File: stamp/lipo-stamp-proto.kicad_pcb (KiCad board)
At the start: 4 copper layers, 17.8 x 17.8 mm, 31 parts, among them IC1 TP4056, Q1 Q_PMOS_GSD, U1 AP2112K-3.3, U2 AP9101CK6, U3 FS8205

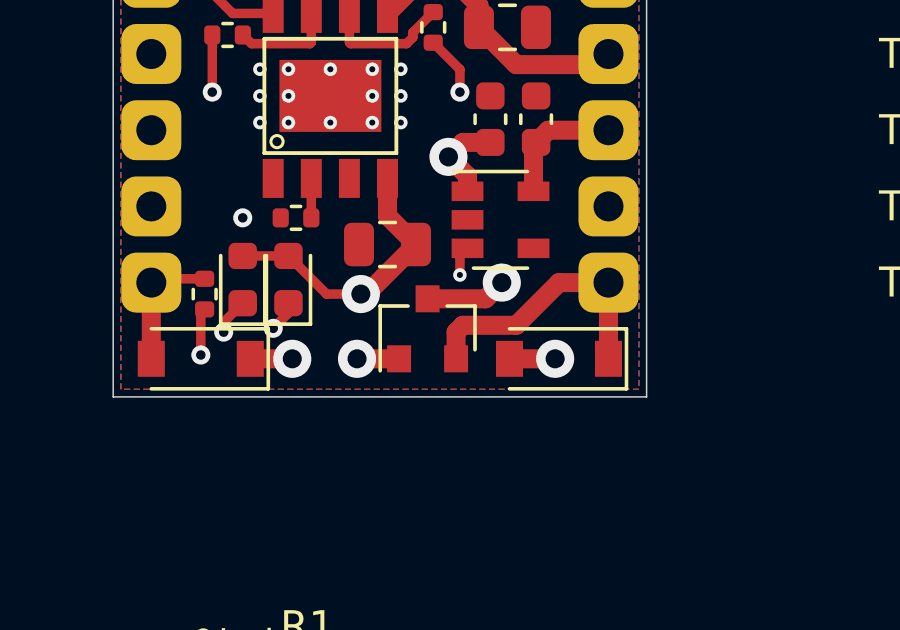
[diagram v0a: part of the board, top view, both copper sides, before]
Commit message: Add fabrication outputs, not jlc corrected yet
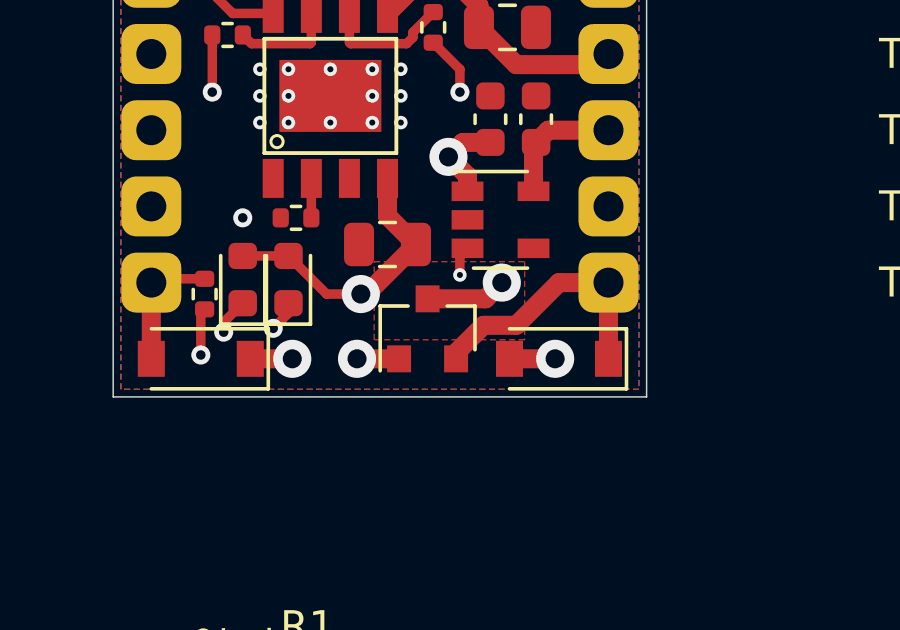
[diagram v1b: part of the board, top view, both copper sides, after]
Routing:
- added copper zone on F.Cu, net /+BATT
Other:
- board text added: "@bitshiftmask"
- board text added: "IN"
- board text added: "JLCJLCJLCJLC"
- board text added: "LiPo Stamp v0.3.0"
- board text added: "OUT"
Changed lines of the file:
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@@
   (general
     (thickness 1.6)
-    (drawings 16)
+    (drawings 31)
     (tracks 163)
     (zones 0)
@@
   )
   (setup
-    (last_trace_width 0.25)
+    (last_trace_width 0.635)
     (user_trace_width 0.2)
     (user_trace_width 0.3175)
@@
       (outputformat 1)
       (mirror false)
-      (drillshape 1)
+      (drillshape 0)
       (scaleselection 1)
-      (outputdirectory ""))
+      (outputdirectory "../fabrication/stamp/"))
   )
   (net 0 "")
@@
   (module Everything:SOP-8 (layer F.Cu)
     (at 115.189 58.547 90)
+    (attr smd)
     (fp_text reference IC1 (at 0.381 -23.241 90) (layer F.SilkS)
       (effects (font (size 1.000283 1.000283) (thickness 0.015)))
@@
     )
   )
+  (gr_text OUT (at 124.079 52.07) (layer B.SilkS)
+    (effects (font (size 1 1) (thickness 0.15)) (justify mirror))
+  )
+  (gr_text IN (at 109.22 52.07) (layer B.SilkS)
+    (effects (font (size 1 1) (thickness 0.15)) (justify mirror))
+  )
+  (gr_line (start 111.506 65.786) (end 122.428 65.786) (layer B.SilkS) (width 0.12))
+  (gr_line (start 111.506 67.564) (end 111.506 65.786) (layer B.SilkS) (width 0.12))
+  (gr_line (start 122.428 67.564) (end 111.506 67.564) (layer B.SilkS) (width 0.12))
+  (gr_line (start 122.428 65.786) (end 122.428 67.564) (layer B.SilkS) (width 0.12))
+  (gr_line (start 114.3 58.42) (end 114.3 53.34) (layer B.SilkS) (width 0.12))
+  (gr_line (start 119.38 58.42) (end 114.3 58.42) (layer B.SilkS) (width 0.12))
+  (gr_line (start 119.38 53.34) (end 119.38 58.42) (layer B.SilkS) (width 0.12))
+  (gr_line (start 111.379 53.34) (end 111.379 51.054) (layer B.SilkS) (width 0.12))
+  (gr_line (start 122.301 53.34) (end 111.379 53.34) (layer B.SilkS) (width 0.12))
+  (gr_line (start 122.301 51.054) (end 122.301 53.34) (layer B.SilkS) (width 0.12))
+  (gr_text @bitshiftmask (at 116.84 66.675) (layer B.SilkS)
+    (effects (font (size 1 1) (thickness 0.15)) (justify mirror))
+  )
+  (gr_text "LiPo\nStamp\nv0.3.0" (at 116.84 55.88) (layer B.SilkS)
+    (effects (font (size 1 1) (thickness 0.15)) (justify mirror))
+  )
+  (gr_text JLCJLCJLCJLC (at 116.84 52.07) (layer B.SilkS)
+    (effects (font (size 1 1) (thickness 0.15)) (justify mirror))
+  )
   (gr_text VMAX (at 123.19 64.77) (layer B.SilkS)
     (effects (font (size 1 1) (thickness 0.15)) (justify left mirror))
@@
     (effects (font (size 1 1) (thickness 0.15)) (justify right mirror))
   )
-  (gr_text B+ (at 110.49 57.15) (layer B.SilkS)
-    (effects (font (size 1 1) (thickness 0.15)) (justify right mirror))
-  )
-  (gr_text B- (at 111.76 54.61) (layer B.SilkS)
-    (effects (font (size 1 1) (thickness 0.15)) (justify right mirror))
+  (gr_text B+ (at 113.665 57.15) (layer B.SilkS)
+    (effects (font (size 1 1) (thickness 0.15)) (justify left mirror))
+  )
+  (gr_text B- (at 113.665 54.61) (layer B.SilkS)
+    (effects (font (size 1 1) (thickness 0.15)) (justify left mirror))
   )
   (gr_line (start 125.73 50.8) (end 107.95 50.8) (layer Edge.Cuts) (width 0.05))
@@
   (segment (start 110.998 64.643) (end 109.347 64.643) (width 0.3175) (layer F.Cu) (net 8))
   (segment (start 124.46 67.31) (end 124.46 64.77) (width 0.635) (layer F.Cu) (net 9))
-  (segment (start 119.38 67.31) (end 119.38 66.421) (width 0.635) (layer F.Cu) (net 9))
-  (segment (start 119.608501 66.192499) (end 121.386501 66.192499) (width 0.635) (layer F.Cu) (net 9))
-  (segment (start 119.38 66.421) (end 119.608501 66.192499) (width 0.635) (layer F.Cu) (net 9))
   (segment (start 122.809 64.77) (end 124.46 64.77) (width 0.635) (layer F.Cu) (net 9))
   (segment (start 121.386501 66.192499) (end 122.809 64.77) (width 0.635) (layer F.Cu) (net 9))
@@
   (segment (start 124.46 64.77) (end 123.317 64.77) (width 1.27) (layer In1.Cu) (net 9))
   (segment (start 123.317 64.77) (end 119.126 60.579) (width 1.27) (layer In1.Cu) (net 9))
+  (segment (start 119.38 67.108498) (end 119.38 67.31) (width 0.635) (layer F.Cu) (net 9))
+  (segment (start 120.295999 66.192499) (end 119.38 67.108498) (width 0.635) (layer F.Cu) (net 9))
+  (segment (start 121.386501 66.192499) (end 120.295999 66.192499) (width 0.635) (layer F.Cu) (net 9))
   (segment (start 109.22 52.126) (end 109.164 52.07) (width 0.635) (layer F.Cu) (net 10))
   (segment (start 109.22 54.61) (end 109.22 52.126) (width 0.635) (layer F.Cu) (net 10))
@@
       )
     )
+  )
+  (zone (net 3) (net_name /+BATT) (layer F.Cu) (hatch edge 0.508)
+    (priority 1)
+    (connect_pads yes (clearance 0.2))
+    (min_thickness 0.254)
+    (fill yes (arc_segments 32) (thermal_gap 0.508) (thermal_bridge_width 0.508))
+    (polygon
+      (pts
+        (xy 121.666 66.675) (xy 116.6495 66.675) (xy 116.6495 64.0715) (xy 121.666 64.0715)
+      )
+    )

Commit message: Update components, regenerate output
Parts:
- Q1: value Q_PMOS_GSD -> SI2301CDS-T1-GE3
- R6: footprint Resistor_SMD:R_0402_1005Metric -> Resistor_SMD:R_0603_1608Metric
- moved R6 0.71 mm to (124.0, 51.8)
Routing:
- net Net-(R6-Pad1): track 5.91 -> 7.07 mm
